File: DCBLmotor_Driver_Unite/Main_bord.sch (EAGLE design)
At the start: 72 parts, among them CN1 DF11-16DP-2DSA, CN2 DF11-16DP-2DSA, CN3 DF11-4DP-2DSR, CN4 HIF3FC-10PA-2.54DSA(71), CN5 HIF3FC-10PA-2.54DSA(71), CN6 0430450612, CN7 0430450612, CN8 BM11B-SRSS-TB, IC1 TMPM370FYFG, IC2 MCP2561FD-E/MF, IC3 AM26C32CD, IC4 AM26C32CD, IC5 LTC2862A, SW1 CVS-02TB, SW2 EVQ-PE104K

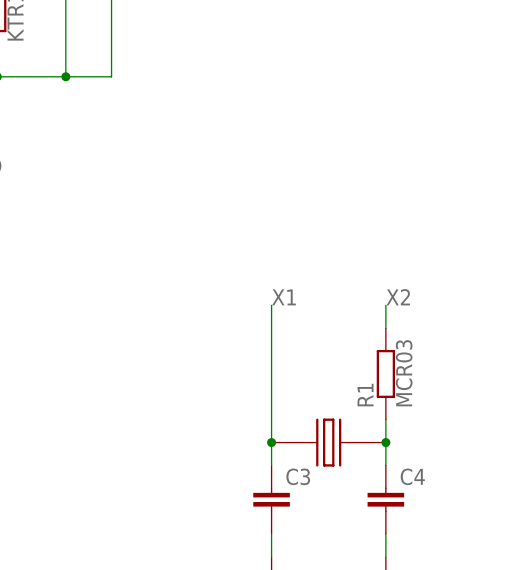
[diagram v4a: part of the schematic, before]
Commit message: Resister for Quartz crystalstal
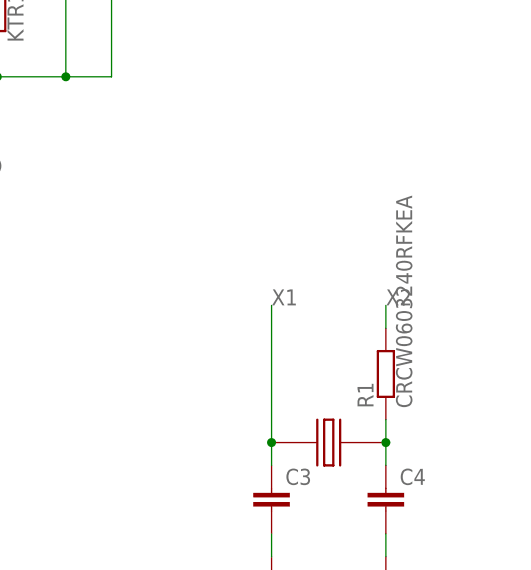
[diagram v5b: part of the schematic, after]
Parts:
- R1: value MCR03 -> CRCW0603240RFKEA; device ROHM:MCR03 -> VISHAY:CRCW0603240RFKEA
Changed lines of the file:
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@@
 <part name="CN1" library="Hirose" deviceset="DF11-16DP-2DSA" device=""/>
 <part name="CN2" library="Hirose" deviceset="DF11-16DP-2DSA" device=""/>
-<part name="R1" library="ROHM" deviceset="MCR03" device=""/>
+<part name="R1" library="VISHAY" deviceset="CRCW0603240RFKEA" device=""/>
 <part name="L1" library="LQW21HN1R0J00L" deviceset="LQW21HN1R0J00L" device=""/>
 <part name="SUPPLY13" library="supply2" library_urn="urn:adsk.eagle:library:372" deviceset="GND" device=""/>

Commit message: fix
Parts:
- R1: value CRCW0603240RFKEA -> CRCW060382R0JNEA; device VISHAY:CRCW0603240RFKEA -> VISHAY:CRCW060382R0JNEA
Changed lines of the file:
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@@
 <part name="CN1" library="Hirose" deviceset="DF11-16DP-2DSA" device=""/>
 <part name="CN2" library="Hirose" deviceset="DF11-16DP-2DSA" device=""/>
-<part name="R1" library="VISHAY" deviceset="CRCW0603240RFKEA" device=""/>
+<part name="R1" library="VISHAY" deviceset="CRCW060382R0JNEA" device=""/>
 <part name="L1" library="LQW21HN1R0J00L" deviceset="LQW21HN1R0J00L" device=""/>
 <part name="SUPPLY13" library="supply2" library_urn="urn:adsk.eagle:library:372" deviceset="GND" device=""/>

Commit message: TEMP Reples parts
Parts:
- DC-DC1: value LTM4622 -> LTM4623IY; device LT:LTM4622 -> LT:LTM4623IY
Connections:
- net +5V: no longer DC-DC1.VOUT1
- net GND: no longer DC-DC1.GND
- net N$10: no longer DC-DC1.FB1
- net N$7: no longer DC-DC1.FB2
- net VCC: no longer DC-DC1.VOUT2
- net VDD: no longer DC-DC1.RUN1, DC-DC1.RUN2, DC-DC1.VIN
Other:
- moved on the sheet: C7, C8, RS1, RS2
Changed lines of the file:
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@@
 <part name="SUPPLY3" library="supply2" library_urn="urn:adsk.eagle:library:372" deviceset="GND" device=""/>
 <part name="SUPPLY5" library="supply2" library_urn="urn:adsk.eagle:library:372" deviceset="GND" device=""/>
-<part name="DC-DC1" library="LT" deviceset="LTM4622" device=""/>
 <part name="RS1" library="ROHM" deviceset="KTR10EZPF1332" device=""/>
 <part name="RS2" library="ROHM" deviceset="KTR10EZPF8251" device=""/>
@@
 <part name="CN10" library="jst-xh" deviceset="B2B-XH-A" device=""/>
 <part name="C5" library="KEMET" deviceset="T356L107K016AT" device=""/>
+<part name="DC-DC1" library="LT" deviceset="LTM4623IY" device=""/>
 </parts>
 <sheets>
@@
 <instance part="SUPPLY1" gate="GND" x="40.64" y="142.24"/>
 <instance part="SUPPLY2" gate="GND" x="231.14" y="20.32"/>
-<instance part="SUPPLY3" gate="GND" x="393.7" y="-17.78"/>
+<instance part="SUPPLY3" gate="GND" x="393.7" y="-22.86"/>
 <instance part="SUPPLY5" gate="GND" x="78.74" y="-127"/>
-<instance part="DC-DC1" gate="G$1" x="378.46" y="50.8"/>
-<instance part="RS1" gate="G$1" x="414.02" y="5.08" rot="R90"/>
-<instance part="RS2" gate="G$1" x="419.1" y="-2.54" rot="R90"/>
-<instance part="SUPPLY8" gate="GND" x="416.56" y="-17.78"/>
-<instance part="C7" gate="G$1" x="426.72" y="20.32"/>
-<instance part="C8" gate="G$1" x="431.8" y="12.7"/>
+<instance part="RS1" gate="G$1" x="429.26" y="5.08" rot="R90"/>
+<instance part="RS2" gate="G$1" x="434.34" y="-2.54" rot="R90"/>
+<instance part="SUPPLY8" gate="GND" x="431.8" y="-17.78"/>
+<instance part="C7" gate="G$1" x="441.96" y="20.32"/>
+<instance part="C8" gate="G$1" x="447.04" y="12.7"/>
 <instance part="CR1" gate="G$1" x="246.38" y="38.1"/>
 <instance part="CR3" gate="G$1" x="231.14" y="30.48"/>
@@
 <instance part="SUPPLY9" gate="GND" x="246.38" y="20.32"/>
 <instance part="SUPPLY10" gate="GND" x="-127" y="7.62"/>
-<instance part="P+6" gate="VCC" x="474.98" y="71.12"/>
-<instance part="P+7" gate="VCC" x="467.36" y="71.12"/>
+<instance part="P+6" gate="VCC" x="490.22" y="71.12"/>
+<instance part="P+7" gate="VCC" x="482.6" y="71.12"/>
 <instance part="SUPPLY4" gate="G$1" x="347.98" y="71.12"/>
 <instance part="SUPPLY11" gate="GND" x="-35.56" y="96.52"/>
@@
 <instance part="CN10" gate="G$1" x="467.36" y="220.98"/>
 <instance part="C5" gate="G$1" x="439.42" y="220.98"/>
+<instance part="DC-DC1" gate="G$1" x="388.62" y="35.56"/>
 </instances>
 <busses>
@@
 <net name="GND" class="0">
 <segment>
-<pinref part="DC-DC1" gate="G$1" pin="GND"/>
 <pinref part="SUPPLY3" gate="GND" pin="GND"/>
-<wire x1="393.7" y1="7.62" x2="393.7" y2="-15.24" width="0.1524" layer="91"/>
+<wire x1="393.7" y1="2.54" x2="393.7" y2="-20.32" width="0.1524" layer="91"/>
 </segment>
 <segment>
 <pinref part="RS1" gate="G$1" pin="2"/>
-<wire x1="414.02" y1="0" x2="414.02" y2="-10.16" width="0.1524" layer="91"/>
+<wire x1="429.26" y1="0" x2="429.26" y2="-10.16" width="0.1524" layer="91"/>
 <pinref part="RS2" gate="G$1" pin="2"/>
-<wire x1="419.1" y1="-7.62" x2="419.1" y2="-10.16" width="0.1524" layer="91"/>
-<wire x1="419.1" y1="-10.16" x2="416.56" y2="-10.16" width="0.1524" layer="91"/>
+<wire x1="434.34" y1="-7.62" x2="434.34" y2="-10.16" width="0.1524" layer="91"/>
+<wire x1="434.34" y1="-10.16" x2="431.8" y2="-10.16" width="0.1524" layer="91"/>
 <pinref part="SUPPLY8" gate="GND" pin="GND"/>
-<wire x1="416.56" y1="-10.16" x2="414.02" y2="-10.16" width="0.1524" layer="91"/>
-<wire x1="416.56" y1="-10.16" x2="416.56" y2="-15.24" width="0.1524" layer="91"/>
-<junction x="416.56" y="-10.16"/>
+<wire x1="431.8" y1="-10.16" x2="429.26" y2="-10.16" width="0.1524" layer="91"/>
+<wire x1="431.8" y1="-10.16" x2="431.8" y2="-15.24" width="0.1524" layer="91"/>
+<junction x="431.8" y="-10.16"/>
 <pinref part="C8" gate="G$1" pin="2"/>
-<wire x1="419.1" y1="-10.16" x2="426.72" y2="-10.16" width="0.1524" layer="91"/>
-<wire x1="426.72" y1="-10.16" x2="431.8" y2="-10.16" width="0.1524" layer="91"/>
-<wire x1="431.8" y1="-10.16" x2="431.8" y2="7.62" width="0.1524" layer="91"/>
-<junction x="419.1" y="-10.16"/>
+<wire x1="434.34" y1="-10.16" x2="441.96" y2="-10.16" width="0.1524" layer="91"/>
+<wire x1="441.96" y1="-10.16" x2="447.04" y2="-10.16" width="0.1524" layer="91"/>
+<wire x1="447.04" y1="-10.16" x2="447.04" y2="7.62" width="0.1524" layer="91"/>
+<junction x="434.34" y="-10.16"/>
 <pinref part="C7" gate="G$1" pin="2"/>
-<wire x1="426.72" y1="15.24" x2="426.72" y2="-10.16" width="0.1524" layer="91"/>
-<junction x="426.72" y="-10.16"/>
+<wire x1="441.96" y1="15.24" x2="441.96" y2="-10.16" width="0.1524" layer="91"/>
+<junction x="441.96" y="-10.16"/>
 </segment>
 <segment>
@@
 <net name="N$7" class="0">
 <segment>
-<pinref part="DC-DC1" gate="G$1" pin="FB2"/>
 <pinref part="RS1" gate="G$1" pin="1"/>
-<wire x1="408.94" y1="17.78" x2="414.02" y2="17.78" width="0.1524" layer="91"/>
-<wire x1="414.02" y1="17.78" x2="414.02" y2="10.16" width="0.1524" layer="91"/>
+<wire x1="421.64" y1="17.78" x2="429.26" y2="17.78" width="0.1524" layer="91"/>
+<wire x1="429.26" y1="17.78" x2="429.26" y2="10.16" width="0.1524" layer="91"/>
 </segment>
 </net>
 <net name="N$10" class="0">
 <segment>
-<pinref part="DC-DC1" gate="G$1" pin="FB1"/>
 <pinref part="RS2" gate="G$1" pin="1"/>
-<wire x1="408.94" y1="22.86" x2="419.1" y2="22.86" width="0.1524" layer="91"/>
-<wire x1="419.1" y1="22.86" x2="419.1" y2="2.54" width="0.1524" layer="91"/>
+<wire x1="421.64" y1="22.86" x2="434.34" y2="22.86" width="0.1524" layer="91"/>
+<wire x1="434.34" y1="22.86" x2="434.34" y2="2.54" width="0.1524" layer="91"/>
 </segment>
 </net>
@@
 <segment>
 <pinref part="P+6" gate="VCC" pin="VCC"/>
-<wire x1="474.98" y1="68.58" x2="474.98" y2="38.1" width="0.1524" layer="91"/>
-<label x="469.9" y="55.88" size="1.778" layer="95"/>
-<wire x1="426.72" y1="38.1" x2="474.98" y2="38.1" width="0.1524" layer="91"/>
+<wire x1="490.22" y1="68.58" x2="490.22" y2="38.1" width="0.1524" layer="91"/>
+<label x="485.14" y="55.88" size="1.778" layer="95"/>
+<wire x1="441.96" y1="38.1" x2="490.22" y2="38.1" width="0.1524" layer="91"/>
 <pinref part="C7" gate="G$1" pin="1"/>
-<pinref part="DC-DC1" gate="G$1" pin="VOUT2"/>
-<wire x1="426.72" y1="22.86" x2="426.72" y2="38.1" width="0.1524" layer="91"/>
-<wire x1="426.72" y1="38.1" x2="408.94" y2="38.1" width="0.1524" layer="91"/>
-<junction x="426.72" y="38.1"/>
+<wire x1="441.96" y1="22.86" x2="441.96" y2="38.1" width="0.1524" layer="91"/>
+<wire x1="441.96" y1="38.1" x2="421.64" y2="38.1" width="0.1524" layer="91"/>
+<junction x="441.96" y="38.1"/>
 </segment>
 <segment>
@@
 <segment>
 <pinref part="P+7" gate="VCC" pin="VCC"/>
-<wire x1="467.36" y1="68.58" x2="467.36" y2="43.18" width="0.1524" layer="91"/>
-<label x="459.74" y="55.88" size="1.778" layer="95"/>
-<pinref part="DC-DC1" gate="G$1" pin="VOUT1"/>
+<wire x1="482.6" y1="68.58" x2="482.6" y2="43.18" width="0.1524" layer="91"/>
+<label x="474.98" y="55.88" size="1.778" layer="95"/>
 <pinref part="C8" gate="G$1" pin="1"/>
-<wire x1="408.94" y1="43.18" x2="431.8" y2="43.18" width="0.1524" layer="91"/>
-<wire x1="431.8" y1="43.18" x2="431.8" y2="15.24" width="0.1524" layer="91"/>
-<junction x="431.8" y="43.18"/>
-<wire x1="431.8" y1="43.18" x2="467.36" y2="43.18" width="0.1524" layer="91"/>
+<wire x1="421.64" y1="43.18" x2="447.04" y2="43.18" width="0.1524" layer="91"/>
+<wire x1="447.04" y1="43.18" x2="447.04" y2="15.24" width="0.1524" layer="91"/>
+<junction x="447.04" y="43.18"/>
+<wire x1="447.04" y1="43.18" x2="482.6" y2="43.18" width="0.1524" layer="91"/>
 </segment>
 <segment>
@@
 <wire x1="347.98" y1="68.58" x2="347.98" y2="50.8" width="0.1524" layer="91"/>
 <label x="353.06" y="63.5" size="1.778" layer="95"/>
-<pinref part="DC-DC1" gate="G$1" pin="VIN"/>
 <wire x1="373.38" y1="50.8" x2="363.22" y2="50.8" width="0.1524" layer="91"/>
-<pinref part="DC-DC1" gate="G$1" pin="RUN2"/>
 <wire x1="363.22" y1="50.8" x2="347.98" y2="50.8" width="0.1524" layer="91"/>
 <wire x1="373.38" y1="40.64" x2="363.22" y2="40.64" width="0.1524" layer="91"/>
 <wire x1="363.22" y1="40.64" x2="363.22" y2="45.72" width="0.1524" layer="91"/>
 <junction x="363.22" y="50.8"/>
-<pinref part="DC-DC1" gate="G$1" pin="RUN1"/>
 <wire x1="363.22" y1="45.72" x2="363.22" y2="50.8" width="0.1524" layer="91"/>
 <wire x1="373.38" y1="45.72" x2="363.22" y2="45.72" width="0.1524" layer="91"/>
